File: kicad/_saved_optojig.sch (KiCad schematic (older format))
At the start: 20 parts, among them Q1 2N2219, Q2 2N2219, SW1 Switch_SPDT_x2, U1 TRN1-0510, U2 LM358

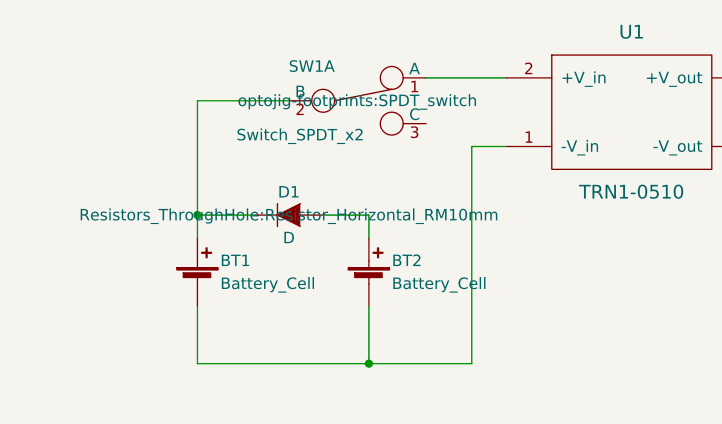
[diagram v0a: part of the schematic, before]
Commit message: Added battery holder datasheet
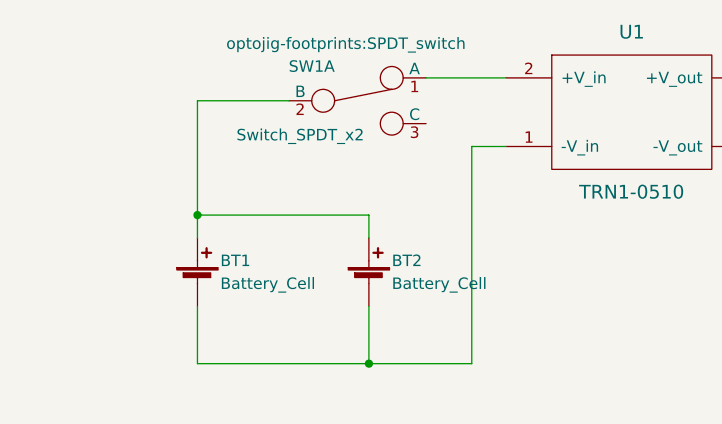
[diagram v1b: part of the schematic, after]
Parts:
- removed D1: D, Resistors_ThroughHole:Resistor_Horizontal_RM10mm, symbol D
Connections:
- net at BT1.1 (+), SW1.2 (B): now also BT2.1 (+)
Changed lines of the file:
@@
 F 0 "SW1" H 1800 3150 50  0000 C CNN
 F 1 "Switch_SPDT_x2" H 1750 2850 50  0000 C CNN
-F 2 "optojig-footprints:SPDT_switch" H 2000 3000 50  0000 C CNN
+F 2 "optojig-footprints:SPDT_switch" H 1950 3250 50  0000 C CNN
 F 3 "" H 2000 3000 50  0000 C CNN
 	1    2000 3000
@@
 $EndComp
 $Comp
-L GND #PWR1
+L GND #PWR01
 U 1 1 5AFD9689
 P 6450 5500
-F 0 "#PWR1" H 6450 5250 50  0001 C CNN
+F 0 "#PWR01" H 6450 5250 50  0001 C CNN
 F 1 "GND" H 6450 5350 50  0000 C CNN
 F 2 "" H 6450 5500 50  0000 C CNN
@@
 	1    0    0    -1
 $EndComp
-$Comp
-L D D1
-U 1 1 5AFE885E
-P 1700 3500
-F 0 "D1" H 1700 3600 50  0000 C CNN
-F 1 "D" H 1700 3400 50  0000 C CNN
-F 2 "Resistors_ThroughHole:Resistor_Horizontal_RM10mm" H 1700 3500 50  0000 C CNN
-F 3 "" H 1700 3500 50  0000 C CNN
-	1    1700 3500
-	1    0    0    -1
-$EndComp
 Wire Wire Line
-	1550 3500 1300 3500
+	1300 3500 2050 3500
 Connection ~ 1300 3500
 Wire Wire Line
-	1850 3500 2050 3500
-Wire Wire Line
 	2050 3500 2050 3600
